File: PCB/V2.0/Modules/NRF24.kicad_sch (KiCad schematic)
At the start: 1 part, among them U3 NRF24L01_Breakout

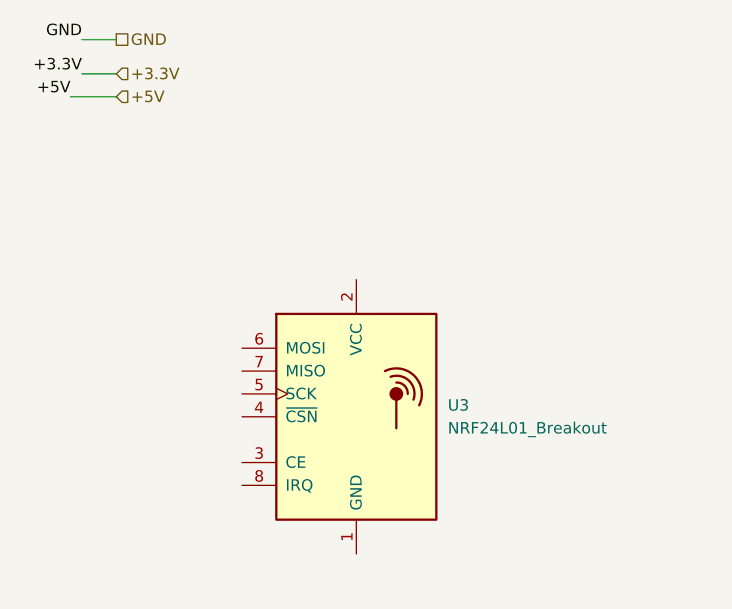
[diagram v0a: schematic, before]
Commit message: Update V2.0 form factor
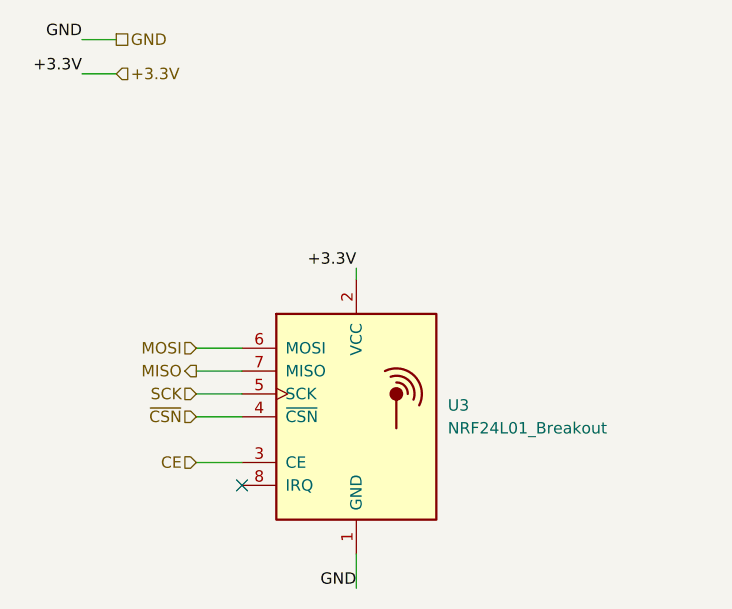
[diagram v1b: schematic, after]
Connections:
- net +3.3V: now also U3.2 (VCC)
- net GND: now also U3.1 (GND)
- net CE: now reaches U3.3 (CE)
- net ~{CSN}: now reaches U3.4 (~{CSN})
- net SCK: now reaches U3.5 (SCK)
- net MOSI: now reaches U3.6 (MOSI)
- net MISO: now reaches U3.7 (MISO)
- no-connect marks 0 -> 1
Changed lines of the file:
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@@
 		(company "Designed by CREPP-NLG")
 	)
-	(wire
-		(pts
-			(xy 25.4 31.75) (xy 30.48 31.75)
+	(no_connect
+		(at 44.45 74.93)
+	)
+	(wire
+		(pts
+			(xy 39.37 67.31) (xy 44.45 67.31)
+		)
+		(stroke
+			(width 0)
+			(type default)
+		)
+	)
+	(wire
+		(pts
+			(xy 57.15 50.8) (xy 57.15 52.07)
+		)
+		(stroke
+			(width 0)
+			(type default)
+		)
+	)
+	(wire
+		(pts
+			(xy 39.37 62.23) (xy 44.45 62.23)
+		)
+		(stroke
+			(width 0)
+			(type default)
+		)
+	)
+	(wire
+		(pts
+			(xy 39.37 72.39) (xy 44.45 72.39)
+		)
+		(stroke
+			(width 0)
+			(type default)
+		)
+	)
+	(wire
+		(pts
+			(xy 39.37 59.69) (xy 44.45 59.69)
+		)
+		(stroke
+			(width 0)
+			(type default)
+		)
+	)
+	(wire
+		(pts
+			(xy 39.37 64.77) (xy 44.45 64.77)
+		)
+		(stroke
+			(width 0)
+			(type default)
+		)
+	)
+	(wire
+		(pts
+			(xy 57.15 82.55) (xy 57.15 86.36)
 		)
 		(stroke
@@
 		)
 	)
-	(label "+5V"
-		(at 25.4 31.75 180)
+	(label "+3.3V"
+		(at 57.15 50.8 180)
 		(fields_autoplaced yes)
 		(effects
@@
 		)
 	)
-	(hierarchical_label "+5V"
-		(shape input)
-		(at 30.48 31.75 0)
-		(fields_autoplaced yes)
-		(effects
-			(font
-				(size 1.27 1.27)
-			)
-			(justify left)
+	(label "GND"
+		(at 57.15 86.36 180)
+		(fields_autoplaced yes)
+		(effects
+			(font
+				(size 1.27 1.27)
+			)
+			(justify right bottom)
+		)
+	)
+	(hierarchical_label "MOSI"
+		(shape input)
+		(at 39.37 59.69 180)
+		(fields_autoplaced yes)
+		(effects
+			(font
+				(size 1.27 1.27)
+			)
+			(justify right)
+		)
+	)
+	(hierarchical_label "CE"
+		(shape input)
+		(at 39.37 72.39 180)
+		(fields_autoplaced yes)
+		(effects
+			(font
+				(size 1.27 1.27)
+			)
+			(justify right)
+		)
+	)
+	(hierarchical_label "~{CSN}"
+		(shape input)
+		(at 39.37 67.31 180)
+		(fields_autoplaced yes)
+		(effects
+			(font
+				(size 1.27 1.27)
+			)
+			(justify right)
 		)
 	)
@@
 		)
 	)
+	(hierarchical_label "SCK"
+		(shape input)
+		(at 39.37 64.77 180)
+		(fields_autoplaced yes)
+		(effects
+			(font
+				(size 1.27 1.27)
+			)
+			(justify right)
+		)
+	)
+	(hierarchical_label "MISO"
+		(shape output)
+		(at 39.37 62.23 180)
+		(fields_autoplaced yes)
+		(effects
+			(font
+				(size 1.27 1.27)
+			)
+			(justify right)
+		)
+	)

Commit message: Update
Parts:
- removed U3: NRF24L01_Breakout, RF_Module:nRF24L01_Breakout, symbol RF:NRF24L01_Breakout
- added U11: ~, CREPP_NRF24:nRF24L01_Virtual, symbol CREPP_NRF24:NRF24_Virtual
- added U3: NRF24L01_Breakout_socket, CREPP_NRF24:nRF24L01_Breakout, symbol CREPP_NRF24:NRF24L01_Breakout _Socket
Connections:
- net +3.3V: now also U3.2 (VCC)
- net CE: now also U3.3 (CE)
- net GND: now also U3.1 (GND)
- net MISO: now also U3.7 (MISO)
- net MOSI: now also U3.6 (MOSI)
- net SCK: now also U3.5 (SCK)
- net ~{CSN}: now also U3.4 (~{CSN})
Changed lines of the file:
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@@
 	)
 	(symbol
-		(lib_id "RF:NRF24L01_Breakout")
+		(lib_id "CREPP_NRF24:NRF24_Virtual")
+		(at 80.01 57.15 0)
+		(unit 1)
+		(exclude_from_sim no)
+		(in_bom yes)
+		(on_board yes)
+		(dnp no)
+		(fields_autoplaced yes)
+		(property "Reference" "U11"
+			(at 86.36 52.0699 0)
+			(effects
+				(font
+					(size 1.27 1.27)
+				)
+				(justify left)
+			)
+		)
+		(property "Value" "~"
+			(at 86.36 53.975 0)
+			(effects
+				(font
+					(size 1.27 1.27)
+				)
+				(justify left)
+			)
+		)
+		(property "Footprint" "CREPP_NRF24:nRF24L01_Virtual"
+			(at 80.01 57.15 0)
+			(effects
+				(font
+					(size 1.27 1.27)
+				)
+				(hide yes)
+			)
+		)
+		(property "Datasheet" ""
+			(at 80.01 57.15 0)
+			(effects
+				(font
+					(size 1.27 1.27)
+				)
+				(hide yes)
+			)
+		)
+		(property "Description" ""
+			(at 80.01 57.15 0)
+			(effects
+				(font
+					(size 1.27 1.27)
+				)
+				(hide yes)
+			)
+		)
+		(instances
+			(project ""
+				(path "/8bcd0d00-b75f-4070-8d50-196a2022a31c/17a13a70-dbe2-4ce7-8cfb-2751d401edd0"
+					(reference "U11")
+					(unit 1)
+				)
+			)
+		)
+	)
+	(symbol
+		(lib_id "CREPP_NRF24:NRF24L01_Breakout _Socket")
 		(at 57.15 67.31 0)
 		(unit 1)
@@
 			)
 		)
-		(property "Value" "NRF24L01_Breakout"
+		(property "Value" "NRF24L01_Breakout_socket"
 			(at 67.31 68.5799 0)
 			(effects
@@
 			)
 		)
-		(property "Footprint" "RF_Module:nRF24L01_Breakout"
+		(property "Footprint" "CREPP_NRF24:nRF24L01_Breakout"
 			(at 60.96 52.07 0)
 			(effects
@@
 			)
 		)
+		(pin "5"
+		)
+		(pin "6"
+		)
+		(pin "8"
+		)
+		(pin "1"
+		)
+		(pin "7"
+		)
+		(pin "4"
+		)
 		(pin "3"
 		)
 		(pin "2"
 		)
-		(pin "1"
-		)
-		(pin "4"
-		)
-		(pin "5"
-		)
-		(pin "6"
-		)
-		(pin "7"
-		)
-		(pin "8"
-		)
 		(instances
